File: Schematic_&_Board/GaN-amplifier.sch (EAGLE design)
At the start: 104 parts, among them IC1 LT3080, J1 JOHNSON_SMA_EDGE_LAUNCH_142-0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, J2 JOHNSON_SMA_EDGE_LAUNCH_142-0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, Q1 MMBT3906LT1SMD, T1 IPB080N03L G, T2 IPB080N03L G, T3 IPB080N03L G, T4 IPB080N03L G, T5 BSP89, U1 TPS7A30XX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

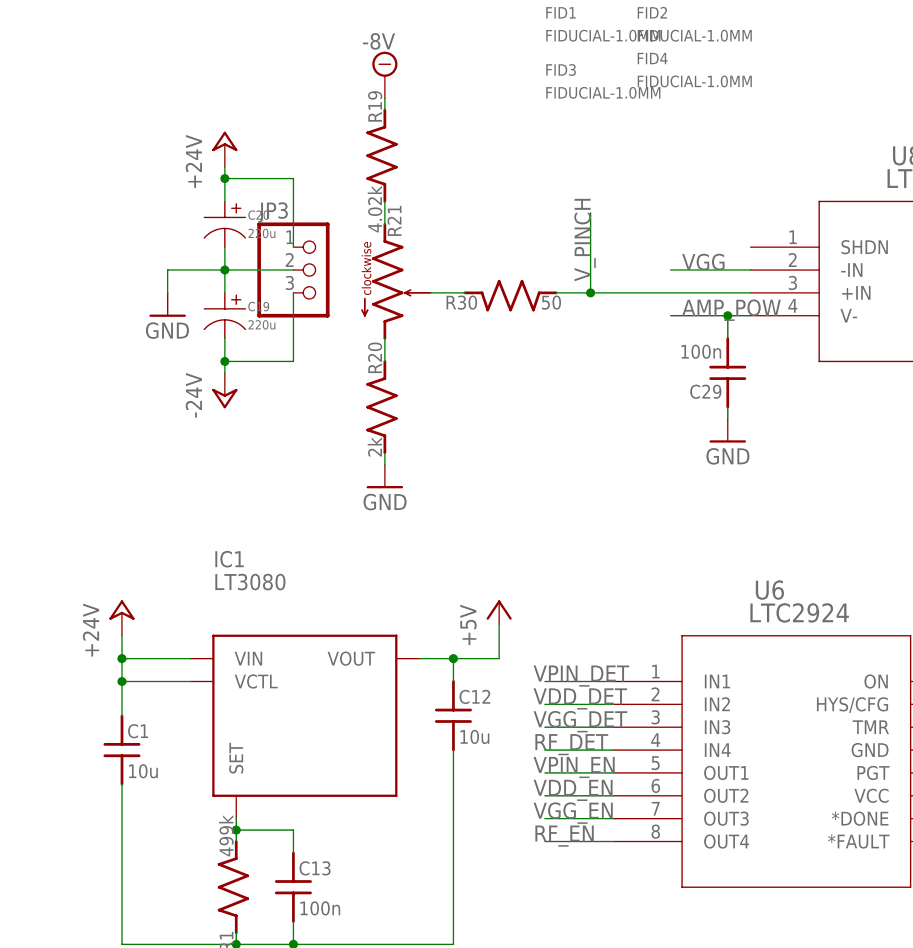
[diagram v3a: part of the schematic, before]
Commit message: Fixes per Alessandro
Added LP-filter for gate voltage and GND plane cutouts to improve RF
performance. Also switched a few components for equivalent parts to
reduce cost.

DSB
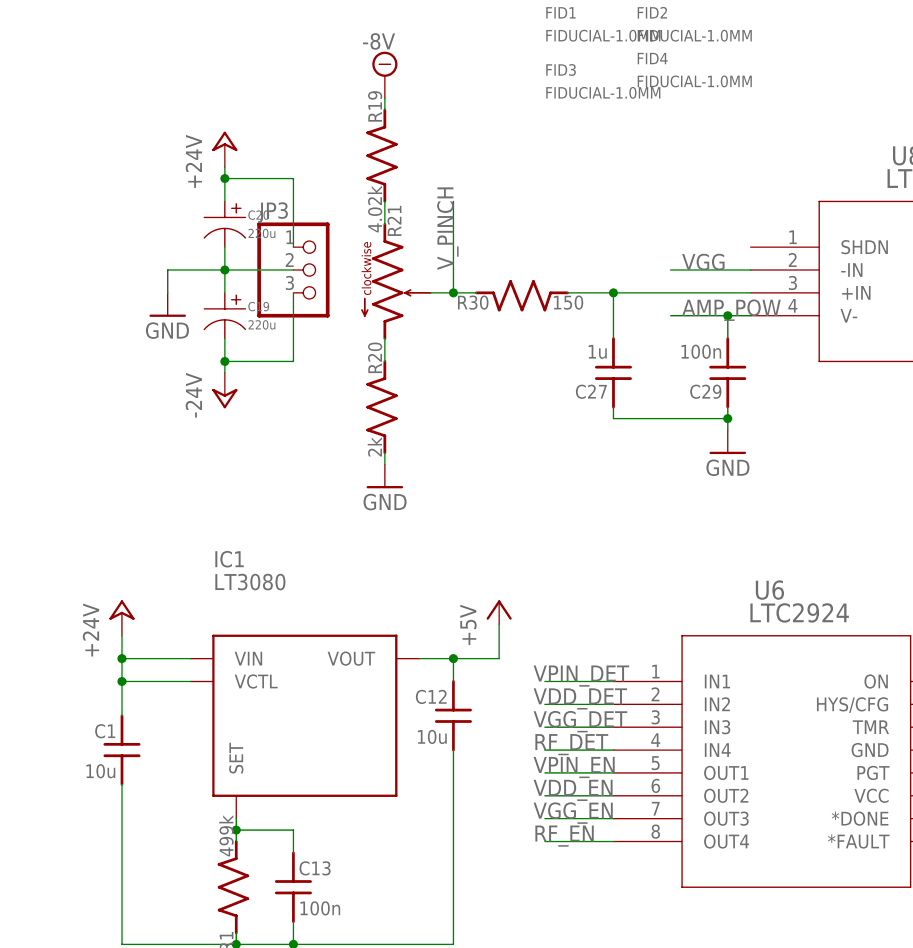
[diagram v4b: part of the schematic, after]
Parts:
- added C27: 1u, jqi_passives:C_MLCC_SMDCMLCC_0603
- C1, C12: device jqi_passives:C_MLCC_SMDCMLCC_0805 -> jqi_passives:C_MLCC_SMDCMLCC_1210; PARTNO C2012X5R1V106K085AC -> UMK325C7106MM-T
- R30: value 50 -> 150; PARTNO ERJ-3EKF49R9V -> ERJ-3EKF1500V
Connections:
- removed net N$36: R21.2, R30.1
- new net N$43: C27.2, R30.2, U8.+IN
- net GND: now also C27.1
- net V_PINCH: now also R21.2, R30.1; no longer R30.2, U8.+IN
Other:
- moved on the sheet: R30
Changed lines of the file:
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@@
 <attribute name="PARTNO" value="LT3080EQ#PBF"/>
-</part>
-<part name="C1" library="jqi_passives" deviceset="C_MLCC_SMD" device="CMLCC_0805" value="10u">
-<attribute name="PARTNO" value="C2012X5R1V106K085AC"/>
 </part>
 <part name="GND1" library="supply1" deviceset="GND" device=""/>
 <part name="R1" library="jqi_passives" deviceset="R_SMD" device="R0603" value="499k">
 <attribute name="PARTNO" value="ERJ-3EKF4993V"/>
-</part>
-<part name="C12" library="jqi_passives" deviceset="C_MLCC_SMD" device="CMLCC_0805" value="10u">
-<attribute name="PARTNO" value="C2012X5R1V106K085AC"/>
 </part>
 <part name="C13" library="jqi_passives" deviceset="C_MLCC_SMD" device="CMLCC_0603" value="100n">
@@
 <attribute name="PARTNO" value="CL10B102KA8NNNC"/>
 </part>
-<part name="R30" library="jqi_passives" deviceset="R_SMD" device="R0603" value="50">
-<attribute name="PARTNO" value="ERJ-3EKF49R9V"/>
+<part name="R30" library="jqi_passives" deviceset="R_SMD" device="R0603" value="150">
+<attribute name="PARTNO" value="ERJ-3EKF1500V"/>
 </part>
 <part name="GND19" library="supply1" deviceset="GND" device=""/>
@@
 <part name="FID7" library="fiducials-jqi" deviceset="FIDUCIAL" device="-1.0MM"/>
 <part name="FID8" library="fiducials-jqi" deviceset="FIDUCIAL" device="-1.0MM"/>
+<part name="C27" library="jqi_passives" deviceset="C_MLCC_SMD" device="CMLCC_0603" value="1u">
+<attribute name="PARTNO" value="CL10B105KA8NNNC"/>
+</part>
+<part name="C1" library="jqi_passives" deviceset="C_MLCC_SMD" device="CMLCC_1210" value="10u">
+<attribute name="PARTNO" value="UMK325C7106MM-T"/>
+</part>
+<part name="C12" library="jqi_passives" deviceset="C_MLCC_SMD" device="CMLCC_1210" value="10u">
+<attribute name="PARTNO" value="UMK325C7106MM-T"/>
+</part>
 </parts>
 <sheets>
@@
 <attribute name="PARTNO" x="-38.1" y="133.35" size="1.778" layer="96" display="off"/>
 </instance>
-<instance part="C1" gate="G$1" x="-53.34" y="129.54">
-<attribute name="PARTNO" x="-53.34" y="129.54" size="1.778" layer="96" display="off"/>
-</instance>
 <instance part="GND1" gate="1" x="-40.64" y="102.87"/>
 <instance part="R1" gate="G$1" x="-40.64" y="113.03" rot="R90">
 <attribute name="PARTNO" x="-40.64" y="113.03" size="1.778" layer="96" display="off"/>
-</instance>
-<instance part="C12" gate="G$1" x="-16.51" y="133.35">
-<attribute name="PARTNO" x="-16.51" y="133.35" size="1.778" layer="96" display="off"/>
 </instance>
 <instance part="C13" gate="G$1" x="-34.29" y="114.3">
@@
 <attribute name="PARTNO" x="64.77" y="172.72" size="1.778" layer="96" display="off"/>
 </instance>
-<instance part="R30" gate="G$1" x="-10.16" y="179.07" rot="MR180">
-<attribute name="PARTNO" x="-10.16" y="179.07" size="1.778" layer="96" display="off"/>
+<instance part="R30" gate="G$1" x="-8.89" y="179.07" rot="MR180">
+<attribute name="PARTNO" x="-8.89" y="179.07" size="1.778" layer="96" display="off"/>
 </instance>
 <instance part="GND19" gate="1" x="64.77" y="182.88" rot="MR0"/>
@@
 <attribute name="PARTNO" x="13.97" y="168.91" size="1.778" layer="96" display="off"/>
 </instance>
-<instance part="GND20" gate="1" x="13.97" y="162.56" rot="MR0"/>
+<instance part="GND20" gate="1" x="13.97" y="161.29" rot="MR0"/>
 <instance part="C19" gate="G$1" x="-41.91" y="176.53">
 <attribute name="PARTNO" x="-41.91" y="176.53" size="1.778" layer="96" display="off"/>
@@
 <instance part="FID7" gate="G$1" x="3.81" y="219.71"/>
 <instance part="FID8" gate="G$1" x="-6.35" y="219.71"/>
+<instance part="C27" gate="G$1" x="1.27" y="168.91" rot="R180">
+<attribute name="PARTNO" x="1.27" y="168.91" size="1.778" layer="96" rot="R90" display="off"/>
+</instance>
+<instance part="C1" gate="G$1" x="-53.34" y="129.54" rot="MR0">
+<attribute name="PARTNO" x="-53.34" y="129.54" size="1.778" layer="96" rot="R90" display="off"/>
+</instance>
+<instance part="C12" gate="G$1" x="-16.51" y="133.35" rot="MR0">
+<attribute name="PARTNO" x="-16.51" y="133.35" size="1.778" layer="96" rot="R90" display="off"/>
+</instance>
 </instances>
 <busses>
@@
 <pinref part="GND1" gate="1" pin="GND"/>
 <wire x1="-40.64" y1="107.95" x2="-40.64" y2="106.68" width="0.1524" layer="91"/>
-<pinref part="C1" gate="G$1" pin="2"/>
 <wire x1="-40.64" y1="106.68" x2="-40.64" y2="105.41" width="0.1524" layer="91"/>
 <wire x1="-53.34" y1="124.46" x2="-53.34" y2="106.68" width="0.1524" layer="91"/>
 <wire x1="-53.34" y1="106.68" x2="-40.64" y2="106.68" width="0.1524" layer="91"/>
 <junction x="-40.64" y="106.68"/>
-<pinref part="C12" gate="G$1" pin="2"/>
 <wire x1="-16.51" y1="128.27" x2="-16.51" y2="106.68" width="0.1524" layer="91"/>
 <wire x1="-16.51" y1="106.68" x2="-34.29" y2="106.68" width="0.1524" layer="91"/>
@@
 <wire x1="-34.29" y1="109.22" x2="-34.29" y2="106.68" width="0.1524" layer="91"/>
 <junction x="-34.29" y="106.68"/>
+<pinref part="C1" gate="G$1" pin="2"/>
+<pinref part="C12" gate="G$1" pin="2"/>
 </segment>
 <segment>
@@
 <pinref part="GND20" gate="1" pin="GND"/>
 <pinref part="C29" gate="G$1" pin="1"/>
+<wire x1="13.97" y1="163.83" x2="13.97" y2="165.1" width="0.1524" layer="91"/>
+<pinref part="C27" gate="G$1" pin="1"/>
 <wire x1="13.97" y1="165.1" x2="13.97" y2="166.37" width="0.1524" layer="91"/>
+<wire x1="1.27" y1="166.37" x2="1.27" y2="165.1" width="0.1524" layer="91"/>
+<wire x1="1.27" y1="165.1" x2="13.97" y2="165.1" width="0.1524" layer="91"/>
+<junction x="13.97" y="165.1"/>
 </segment>
 <segment>
@@
 <wire x1="-53.34" y1="135.89" x2="-45.72" y2="135.89" width="0.1524" layer="91"/>
 <junction x="-53.34" y="138.43"/>
-<pinref part="C1" gate="G$1" pin="1"/>
 <wire x1="-53.34" y1="135.89" x2="-53.34" y2="132.08" width="0.1524" layer="91"/>
 <junction x="-53.34" y="135.89"/>
+<pinref part="C1" gate="G$1" pin="1"/>
 </segment>
 <segment>
@@
 <segment>
 <pinref part="IC1" gate="G$1" pin="VOUT"/>
-<pinref part="C12" gate="G$1" pin="1"/>
 <wire x1="-20.32" y1="138.43" x2="-16.51" y2="138.43" width="0.1524" layer="91"/>
 <wire x1="-16.51" y1="138.43" x2="-16.51" y2="135.89" width="0.1524" layer="91"/>
@@
 <wire x1="-11.43" y1="138.43" x2="-16.51" y2="138.43" width="0.1524" layer="91"/>
 <junction x="-16.51" y="138.43"/>
+<pinref part="C12" gate="G$1" pin="1"/>
 </segment>
 <segment>
@@
 </segment>
 <segment>
-<pinref part="R30" gate="G$1" pin="2"/>
-<wire x1="-5.08" y1="179.07" x2="-1.27" y2="179.07" width="0.1524" layer="91"/>
-<wire x1="-1.27" y1="179.07" x2="-1.27" y2="187.96" width="0.1524" layer="91"/>
-<label x="-1.27" y="180.34" size="1.778" layer="95" rot="R90"/>
-<pinref part="U8" gate="A" pin="+IN"/>
-<wire x1="-1.27" y1="179.07" x2="16.51" y2="179.07" width="0.1524" layer="91"/>
-<junction x="-1.27" y="179.07"/>
+<wire x1="-16.51" y1="179.07" x2="-16.51" y2="189.23" width="0.1524" layer="91"/>
+<label x="-16.51" y="181.61" size="1.778" layer="95" rot="R90"/>
+<pinref part="R21" gate="G$1" pin="2"/>
+<pinref part="R30" gate="G$1" pin="1"/>
+<wire x1="-19.05" y1="179.07" x2="-16.51" y2="179.07" width="0.1524" layer="91"/>
+<wire x1="-16.51" y1="179.07" x2="-13.97" y2="179.07" width="0.1524" layer="91"/>
+<junction x="-16.51" y="179.07"/>
 </segment>
 </net>
@@
 </segment>
 </net>
-<net name="N$36" class="0">
-<segment>
-<pinref part="R21" gate="G$1" pin="2"/>
-<pinref part="R30" gate="G$1" pin="1"/>
-<wire x1="-19.05" y1="179.07" x2="-15.24" y2="179.07" width="0.1524" layer="91"/>
-</segment>
-</net>
 <net name="N$2" class="0">
 <segment>
@@
 </segment>
 </net>
+<net name="N$43" class="0">
+<segment>
+<pinref part="R30" gate="G$1" pin="2"/>
+<pinref part="U8" gate="A" pin="+IN"/>
+<wire x1="-3.81" y1="179.07" x2="1.27" y2="179.07" width="0.1524" layer="91"/>
+<pinref part="C27" gate="G$1" pin="2"/>
+<wire x1="1.27" y1="179.07" x2="16.51" y2="179.07" width="0.1524" layer="91"/>
+<wire x1="1.27" y1="173.99" x2="1.27" y2="179.07" width="0.1524" layer="91"/>
+<junction x="1.27" y="179.07"/>
+</segment>
+</net>

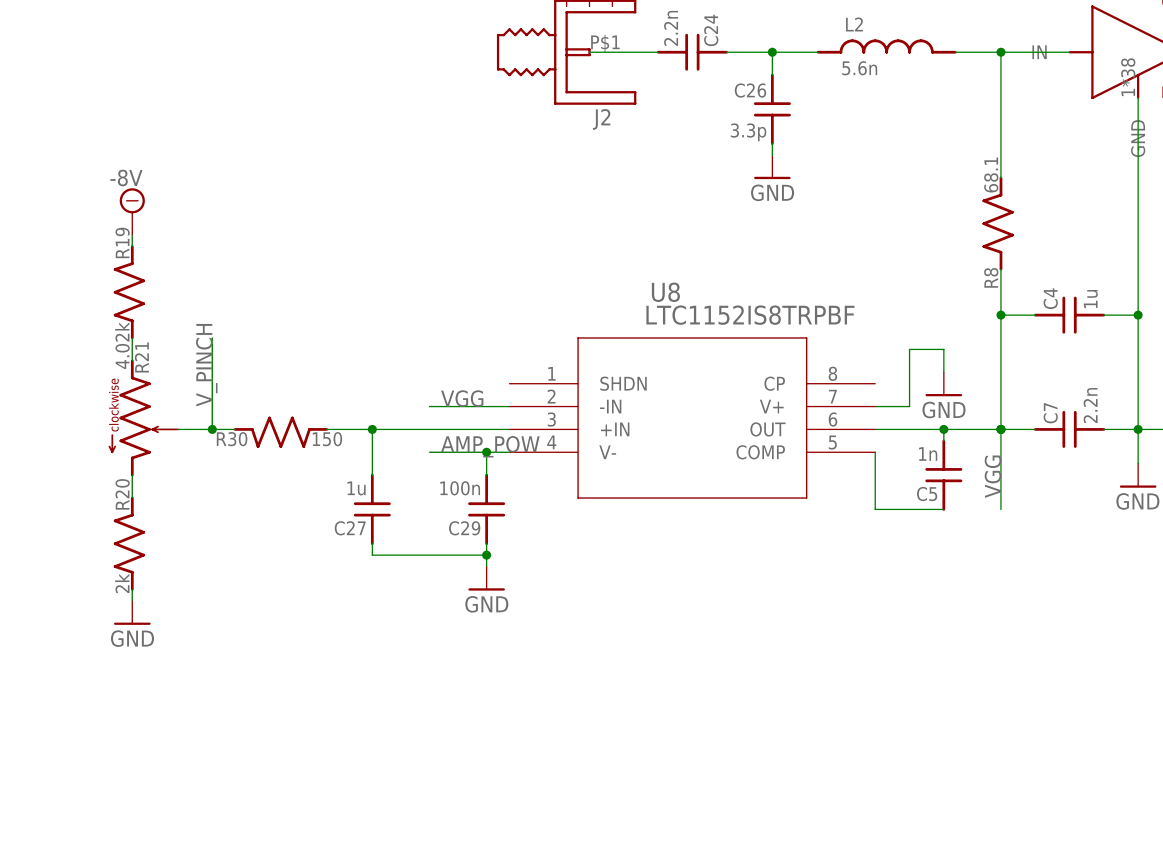
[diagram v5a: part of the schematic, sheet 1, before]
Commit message: New Vgg Buffer
Changed out the Vgg buffer IC to reduce noise.

DSB
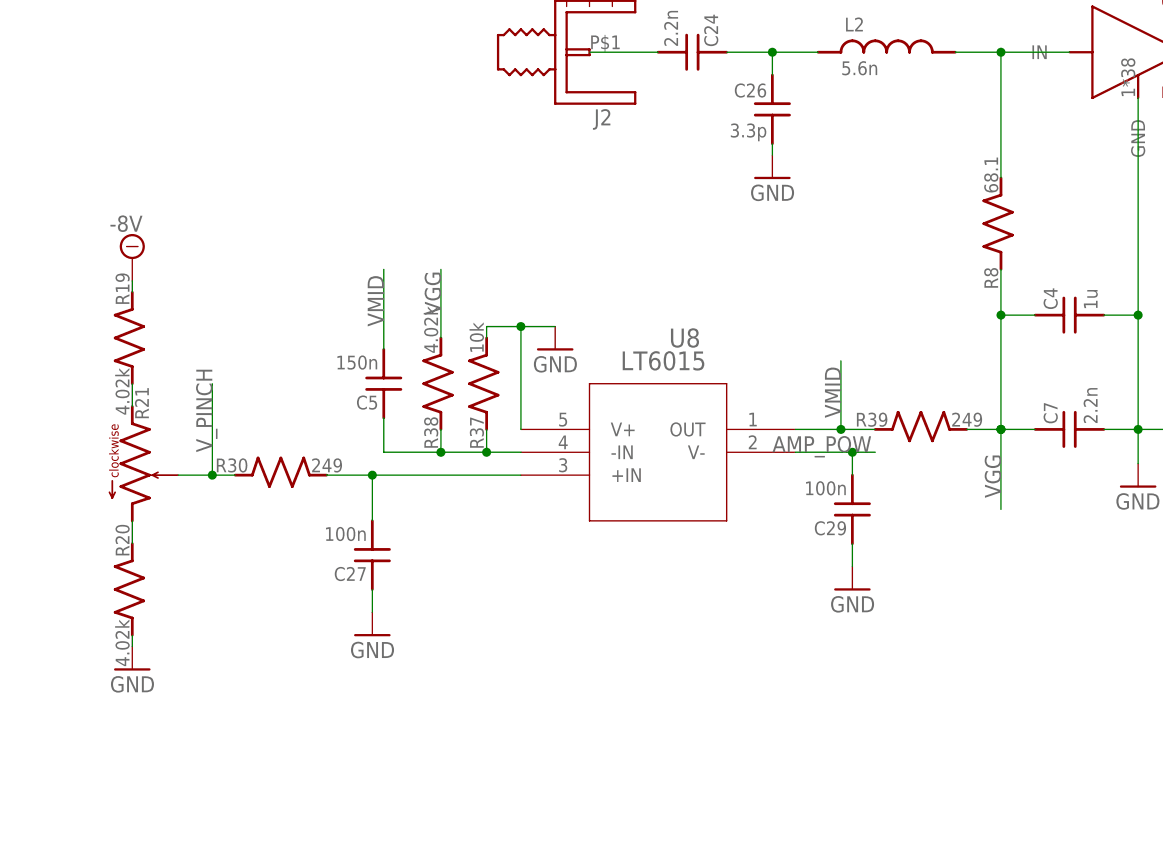
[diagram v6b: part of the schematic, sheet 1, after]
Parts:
- added R37: 10k, jqi_passives:R_SMDR0603
- added R38: 4.02k, jqi_passives:R_SMDR0603
- added R39: 249, jqi_passives:R_SMDR0603
- C27: value 1u -> 100n; PARTNO CL10B105KA8NNNC -> CL10B104KB8SFNC
- C5: value 1n -> 150n; PARTNO CL10B102KA8NNNC -> CL10B154KO8NNNC
- R20: value 2k -> 4.02k; PARTNO TNPW06032K00BXEN -> TNPW06034K02BEEA
- R30: value 150 -> 249; PARTNO ERJ-3EKF1500V -> TNPW0603249RBEEA
- U8: value LTC1152IS8TRPBF -> LT6015; device linear-technology-jqi:LTC1152IS8TRPBF -> linear-technology-jqi:LT6015HS5; PARTNO LTC1152IS8#PBF -> LT6015HS5#TRMPBF
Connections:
- new net VMID: C5.2, R39.1, U8.OUT
- net GND: now also R37.2
- net N$32: now also R37.1, R38.1, U8.-IN; no longer U8.COMP
- net VGG: now also R38.2, R39.2; no longer C5.2, U8.-IN, U8.OUT
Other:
- moved on the sheet: C27, C29, C5, R19, R20, R21, R30

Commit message: Fixed U4 package
Updated board layout with correct optomos package.

DSB
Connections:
- net -8V: now also U4.L+; no longer U4.P$4
- net GND: now also U4.C-; no longer U4.P$2
- net N$16: now also U4.C+; no longer U4.P$1
- net V_PINCH: now also U4.L-; no longer U4.P$3
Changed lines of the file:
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@@
 </segment>
 <segment>
-<pinref part="U4" gate="G$1" pin="P$2"/>
+<pinref part="U4" gate="G$1" pin="C-"/>
 <pinref part="GND11" gate="1" pin="GND"/>
 <wire x1="236.22" y1="69.85" x2="233.68" y2="69.85" width="0.1524" layer="91"/>
@@
 <segment>
 <pinref part="SUPPLY2" gate="G$1" pin="-8V"/>
-<pinref part="U4" gate="G$1" pin="P$4"/>
+<pinref part="U4" gate="G$1" pin="L+"/>
 <wire x1="255.27" y1="85.09" x2="255.27" y2="80.01" width="0.1524" layer="91"/>
 <wire x1="255.27" y1="80.01" x2="251.46" y2="80.01" width="0.1524" layer="91"/>
@@
 <segment>
 <pinref part="R16" gate="G$1" pin="1"/>
-<pinref part="U4" gate="G$1" pin="P$1"/>
+<pinref part="U4" gate="G$1" pin="C+"/>
 <wire x1="232.41" y1="80.01" x2="236.22" y2="80.01" width="0.1524" layer="91"/>
 </segment>
@@
 <net name="V_PINCH" class="0">
 <segment>
-<pinref part="U4" gate="G$1" pin="P$3"/>
+<pinref part="U4" gate="G$1" pin="L-"/>
 <wire x1="251.46" y1="69.85" x2="257.81" y2="69.85" width="0.1524" layer="91"/>
 <label x="252.73" y="69.85" size="1.778" layer="95"/>
